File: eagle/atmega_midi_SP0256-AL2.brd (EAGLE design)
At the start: 100 x 80 mm, 42 parts, among them U1 6N138, U2 ATMEGA328P_PDIP, U3 SP0256-AL2, U4 TL072P

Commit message: layout adjusting
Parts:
- added RESET2: LSP11, solpad:LSP11
- RESET: value 22-23-2021 -> LSP11; device con-molex:22-23-2021 -> solpad:LSP11
- moved C4 42.4 mm to (48.3, 8.89), turned to 0 degrees
- moved C10 27.3 mm to (48.3, 22.9), turned to 0 degrees
- moved R3 17.3 mm to (21.6, 26.7), turned to 90 degrees
- moved VEL_LED 13.5 mm to (87.6, 31.8), turned to 0 degrees
- moved OUTPUT 12.7 mm to (86.4, 0.00)
- moved AMT 12.7 mm to (62.2, 3.81)
- moved C15 12.0 mm to (88.9, 44.5), turned to 0 degrees
- moved R4 10.9 mm to (87.6, 54.6)
- moved Q2 8.13 mm to (83.8, 41.9), turned to 90 degrees
- moved R10 8.03 mm to (63.5, 10.2)
- moved C14 6.48 mm to (88.9, 39.4), turned to 0 degrees
- moved R9 6.35 mm to (40.6, 19.1), turned to 90 degrees
- moved U3 6.35 mm to (61.0, 50.8)
- moved C1 4.02 mm to (55.9, 22.9)
- moved Q1 4.02 mm to (63.5, 22.9)
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- renumbered U$4 to MIDI_IN
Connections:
- net GND: now also MIDI_IN.PE, MIDI_IN.PE1, MIDI_IN.PE2, MIDI_IN.PE@
- net N$15: now also U2.18, U3.P$20; no longer U2.5, U3.P$19
- net N$27: now also U2.19, U3.P$19; no longer U2.4, U3.P$20
- net N$28: now also U2.15; no longer U2.18
- net N$29: now also RESET2.MP; no longer RESET.2
- net N$43: now also RESET.MP; no longer RESET.1

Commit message: 93pct auto
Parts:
- moved R10 10.2 mm to (73.7, 10.2), turned to 270 degrees
- moved C10 9.25 mm to (57.1, 20.3), turned to 180 degrees
- moved C4 6.35 mm to (41.9, 8.89), turned to 180 degrees
- moved C12 4.58 mm to (30.5, 49.5), turned to 180 degrees
- moved U$1 4.58 mm to (3.81, 41.9), turned to 270 degrees
- moved R1 4.02 mm to (25.4, 35.6)
- moved R13 4.02 mm to (30.5, 22.9)
- moved R2 3.81 mm to (16.5, 19.1)
- moved U$2 3.81 mm to (16.5, 41.9), turned to 270 degrees
- moved R26 3.81 mm to (30.5, 19.1)
- moved R24 3.59 mm to (66.0, 20.3)
- moved C3 3.59 mm to (31.8, 34.3)
- moved D1 2.84 mm to (3.81, 26.7)
- moved U2 2.84 mm to (52.1, 33.0)
- moved C1 2.84 mm to (53.3, 24.1), turned to 0 degrees
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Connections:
- removed net N$1: C4.2, C7.1
- net GND: now also C4.2, C7.1, GATE.P$1, OUTPUT.P$1, R13.2, RESET2.MP, U1.5
- net N$28: now also U2.17; no longer U2.15
- net N$29: no longer GATE.P$1, OUTPUT.P$1, R13.2, RESET2.MP, U1.5

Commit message: routed
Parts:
- added C16: 100n, rcl:C025-030X050
- C10, C12, C3, C7, C8: device rcl:C050-024X044 -> rcl:C025-030X050
- moved RESET2 25.7 mm to (26.7, 24.1)
- moved U$2 5.24 mm to (21.6, 43.2)
- moved C12 5.24 mm to (31.8, 44.5), turned to 270 degrees
- moved C7 5.24 mm to (10.2, 41.9), turned to 270 degrees
- moved C5 4.02 mm to (17.8, 43.2)
- moved R1 2.84 mm to (24.1, 33.0)
- moved D1 2.69 mm to (5.71, 28.6)
- moved R4 2.55 mm to (85.1, 56.1)
- moved R13 2.54 mm to (33.0, 22.9)
- moved R26 2.54 mm to (33.0, 19.1)
- moved R2 2.54 mm to (14.0, 19.1)
- moved AMT 2.54 mm to (61.0, 3.81)
- moved R10 2.54 mm to (71.1, 10.2)
- moved C15 1.80 mm to (87.6, 45.7)
- moved C9 1.80 mm to (6.35, 43.2)
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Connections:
- removed net N$29: C1.1, C10.1, C11.-, C12.2, C2.1, C3.2, C5.-, C8.2, C9.+, PWR1.3, PWR1.4, PWR1.5, PWR1.6, PWR1.7, PWR1.8, U2.22, U2.8
- net +5V: now also C16.1
- net GND: now also C1.1, C10.1, C11.-, C12.2, C16.2, C2.1, C3.2, C5.-, C8.2, C9.+, PWR1.3, PWR1.4, PWR1.5, PWR1.6, PWR1.7, PWR1.8, U2.22, U2.8
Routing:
- net GND: track 0.00 -> 469.7 mm, vias 0 -> 2
- net +5V: track 0.00 -> 149.7 mm
- net -12V: track 0.00 -> 101.6 mm
- net N$6: track 0.00 -> 72.9 mm
- net +12V: track 0.00 -> 72.1 mm
- net N$26: track 0.00 -> 32.6 mm
- net N$13: track 0.00 -> 28.8 mm
- net N$25: track 0.00 -> 24.2 mm
- net N$7: track 0.00 -> 23.9 mm
- net N$28: track 0.00 -> 23.6 mm
- net N$30: track 0.00 -> 22.4 mm
- net N$3: track 0.00 -> 21.7 mm
- net N$12: track 0.00 -> 21.6 mm
- net N$5: track 0.00 -> 18.0 mm
- net N$17: track 0.00 -> 17.5 mm
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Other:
- board size 100 x 80 mm -> 101 x 81 mm

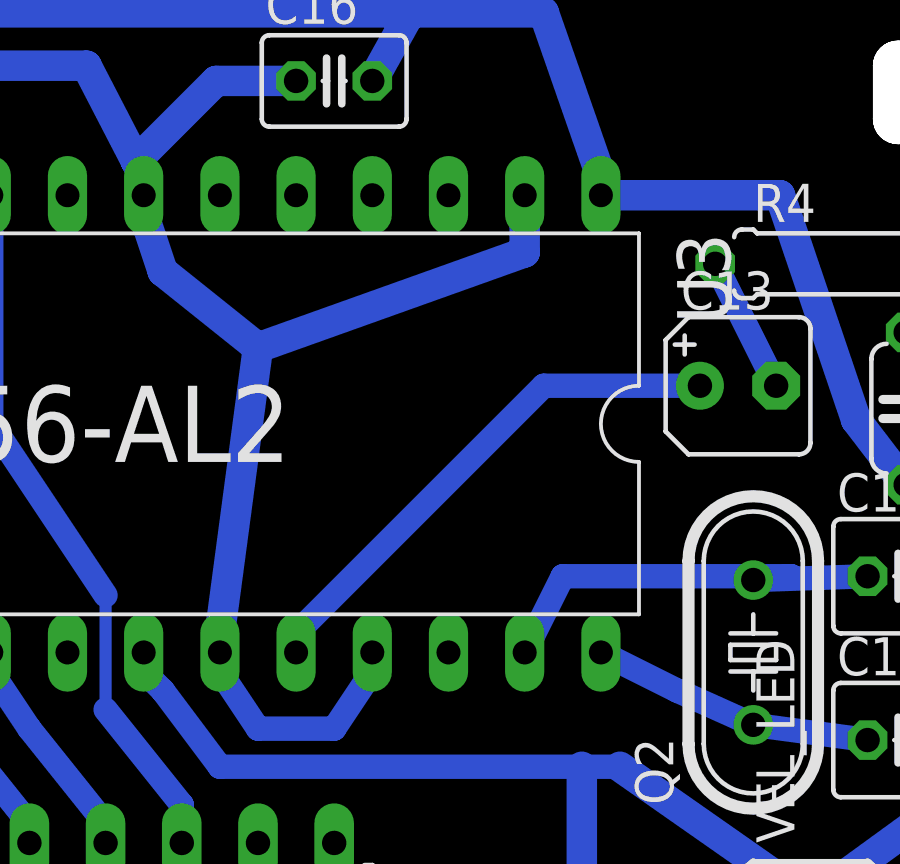
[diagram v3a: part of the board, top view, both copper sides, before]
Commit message: schematic corrected for reset control
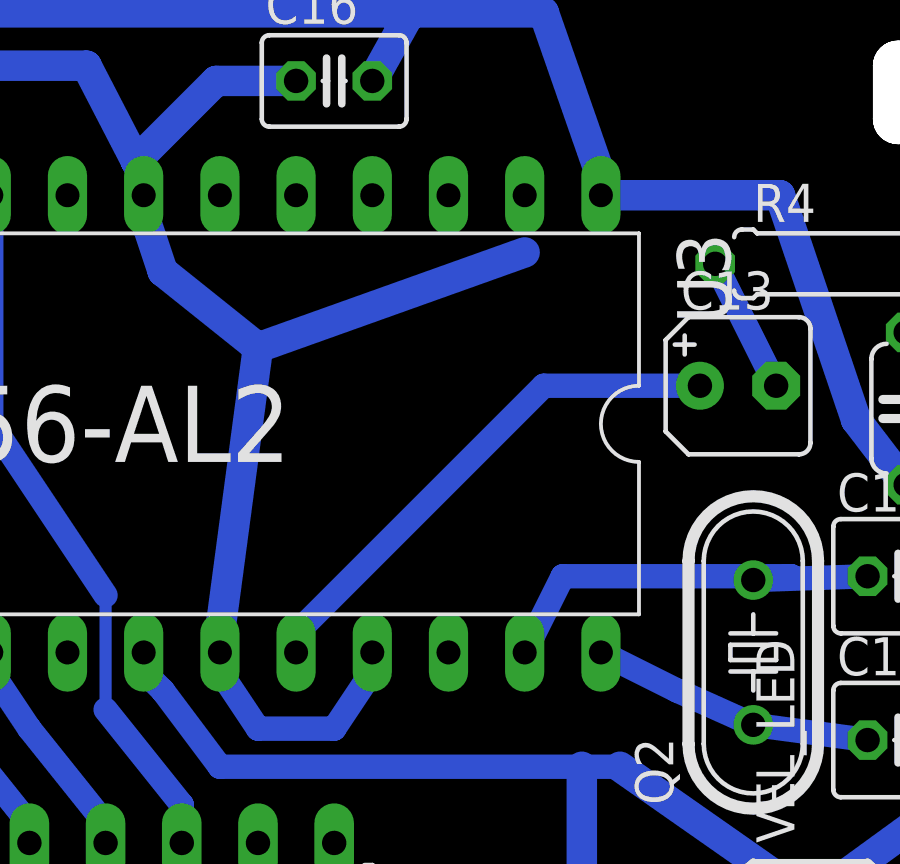
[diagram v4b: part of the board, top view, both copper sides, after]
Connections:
- new net N$1: U2.15, U3.P$2, U3.P$25
- net +5V: no longer U3.P$2, U3.P$25
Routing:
- net +5V: track 149.7 -> 147.1 mm
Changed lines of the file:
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@@
 <contactref element="C12" pad="1"/>
 <contactref element="U3" pad="P$7"/>
-<contactref element="U3" pad="P$2"/>
 <contactref element="U3" pad="P$23"/>
-<contactref element="U3" pad="P$25"/>
 <wire x1="64.77" y1="43.815" x2="64.77" y2="43.18" width="0.8128" layer="16"/>
 <wire x1="62.865" y1="55.88" x2="66.04" y2="53.34" width="1.016" layer="16"/>
@@
 <wire x1="62.23" y1="57.785" x2="62.865" y2="55.88" width="1.016" layer="16"/>
 <wire x1="62.23" y1="58.42" x2="62.23" y2="57.785" width="0.8128" layer="16"/>
-<wire x1="69.85" y1="42.545" x2="69.85" y2="43.18" width="0.8128" layer="16"/>
 <wire x1="68.58" y1="40.64" x2="69.85" y2="42.545" width="0.8128" layer="16"/>
 <wire x1="66.04" y1="40.64" x2="68.58" y2="40.64" width="0.8128" layer="16"/>
 <wire x1="64.77" y1="42.545" x2="66.04" y2="40.64" width="0.8128" layer="16"/>
 <wire x1="64.77" y1="43.18" x2="64.77" y2="42.545" width="0.8128" layer="16"/>
-<wire x1="74.93" y1="56.515" x2="74.93" y2="58.42" width="1.016" layer="16"/>
 <wire x1="66.04" y1="53.34" x2="74.93" y2="56.515" width="1.016" layer="16"/>
 <wire x1="28.194" y1="45.974" x2="30.48" y2="46.99" width="1.016" layer="16"/>
@@
 <wire x1="58.42" y1="36.83" x2="58.42" y2="37.465" width="0.8128" layer="16"/>
 </signal>
+<signal name="N$1">
+<contactref element="U2" pad="15"/>
+<contactref element="U3" pad="P$2"/>
+<contactref element="U3" pad="P$25"/>
+<wire x1="69.85" y1="43.18" x2="74.93" y2="58.42" width="0" layer="19" extent="1-1"/>
+<wire x1="68.58" y1="36.83" x2="69.85" y2="43.18" width="0" layer="19" extent="1-1"/>
+</signal>
 </signals>

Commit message: board corrected for reset control
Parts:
- moved C6 1.63 mm to (88.9, 50.3)
- moved C13 1.37 mm to (81.5, 50.8)
- moved R4 1.27 mm to (85.1, 54.9)
- moved Q2 1.05 mm to (82.3, 42.2)
- moved C15 1.02 mm to (87.6, 44.7)
- moved VEL_LED 0.57 mm to (84.2, 33.1)
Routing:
- net GND: track 469.7 -> 381.0 mm, vias 2 -> 4
- net N$1: track 0.00 -> 44.8 mm
- net +5V: track 147.1 -> 129.6 mm
- net N$6: track 72.9 -> 70.6 mm
- net N$39: track 15.5 -> 16.4 mm
- net N$28: track 23.6 -> 22.8 mm
- net N$38: track 9.47 -> 10.1 mm
- net N$17: track 17.5 -> 18.1 mm
